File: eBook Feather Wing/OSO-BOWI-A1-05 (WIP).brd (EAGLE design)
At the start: 77.5 x 112.3 mm, 100 parts, among them IC1 MCP23008/SO, IC2 23K256-I/SN, J1 SJ-43514-SMT, Q1 IRLML0100, SW1 SPDT_SWITCH

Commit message: rename alt buttons DNP
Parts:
- renumbered BTN_NEXT_ALT to DNP_NEXT_ALT, BTN_PREV_ALT to DNP_PREV_ALT
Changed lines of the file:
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@@
 <attribute name="VALUE" x="32.9565" y="78.232" size="0.508" layer="28" font="vector" ratio="18" rot="MR270" align="center"/>
 </element>
-<element name="BTN_PREV_ALT" library="My Stuff" package="TL3330AF130QG" value="SPST_TACTILE_SWITCHRA" x="2.6416" y="91.44" smashed="yes" rot="MR90">
+<element name="DNP_PREV_ALT" library="My Stuff" package="TL3330AF130QG" value="SPST_TACTILE_SWITCHRA" x="2.6416" y="91.44" smashed="yes" rot="MR90">
 <attribute name="NAME" x="1.6256" y="95.25" size="0.508" layer="52" font="vector" ratio="18" rot="MR90" align="center"/>
 </element>
@@
 <attribute name="VALUE" x="48.768" y="64.008" size="0.4064" layer="28" ratio="10" rot="MR0"/>
 </element>
-<element name="BTN_NEXT_ALT" library="My Stuff" package="TL3330AF130QG" value="SPST_TACTILE_SWITCHRA" x="74.3204" y="90.8558" smashed="yes" rot="MR270">
+<element name="DNP_NEXT_ALT" library="My Stuff" package="TL3330AF130QG" value="SPST_TACTILE_SWITCHRA" x="74.3204" y="90.8558" smashed="yes" rot="MR270">
 <attribute name="NAME" x="75.5904" y="87.0458" size="0.508" layer="52" font="vector" ratio="18" rot="MR270" align="center"/>
 </element>
@@
 <contactref element="JP1" pad="2"/>
 <via x="45.72" y="43.18" extent="1-16" drill="0.254"/>
-<contactref element="BTN_PREV_ALT" pad="P$2"/>
-<contactref element="BTN_NEXT_ALT" pad="P$2"/>
+<contactref element="DNP_PREV_ALT" pad="P$2"/>
+<contactref element="DNP_NEXT_ALT" pad="P$2"/>
 <via x="4.572" y="18.2372" extent="1-16" drill="0.254"/>
 <via x="18.542" y="11.43" extent="1-16" drill="0.254"/>
@@
 <signal name="BTN_NEXT">
 <contactref element="IC1" pad="16"/>
-<contactref element="BTN_NEXT_ALT" pad="P$1"/>
+<contactref element="DNP_NEXT_ALT" pad="P$1"/>
 <wire x1="74.0918" y1="25.5778" x2="72.6812" y2="25.5778" width="0.1524" layer="16"/>
 <wire x1="72.6812" y1="25.5778" x2="72.672" y2="25.587" width="0.1524" layer="16"/>
@@
 </signal>
 <signal name="BTN_PREV">
-<contactref element="BTN_PREV_ALT" pad="P$1"/>
+<contactref element="DNP_PREV_ALT" pad="P$1"/>
 <contactref element="IC1" pad="15"/>
 <wire x1="2.2956" y1="93.34" x2="2.2956" y2="91.3226" width="0.1524" layer="16"/>

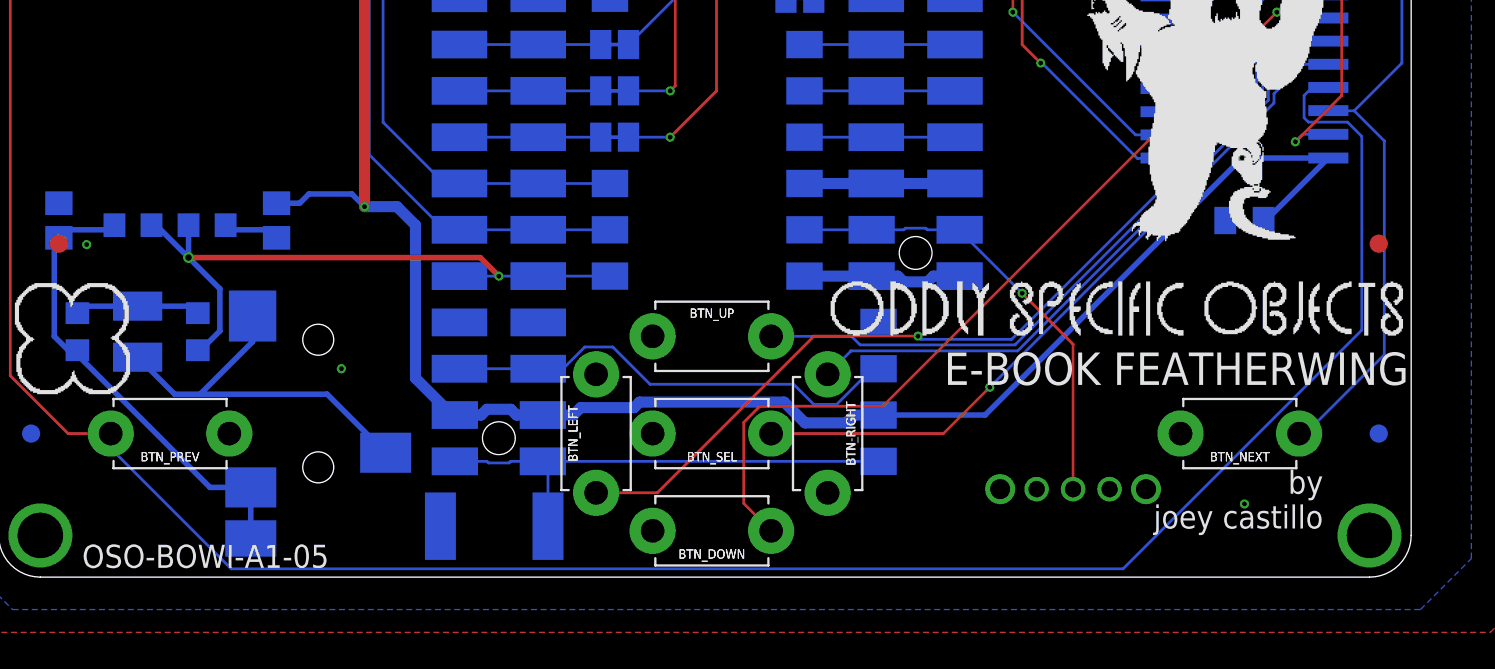
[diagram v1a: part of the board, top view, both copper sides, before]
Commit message: wing: minor silkscreen and routing tweaks
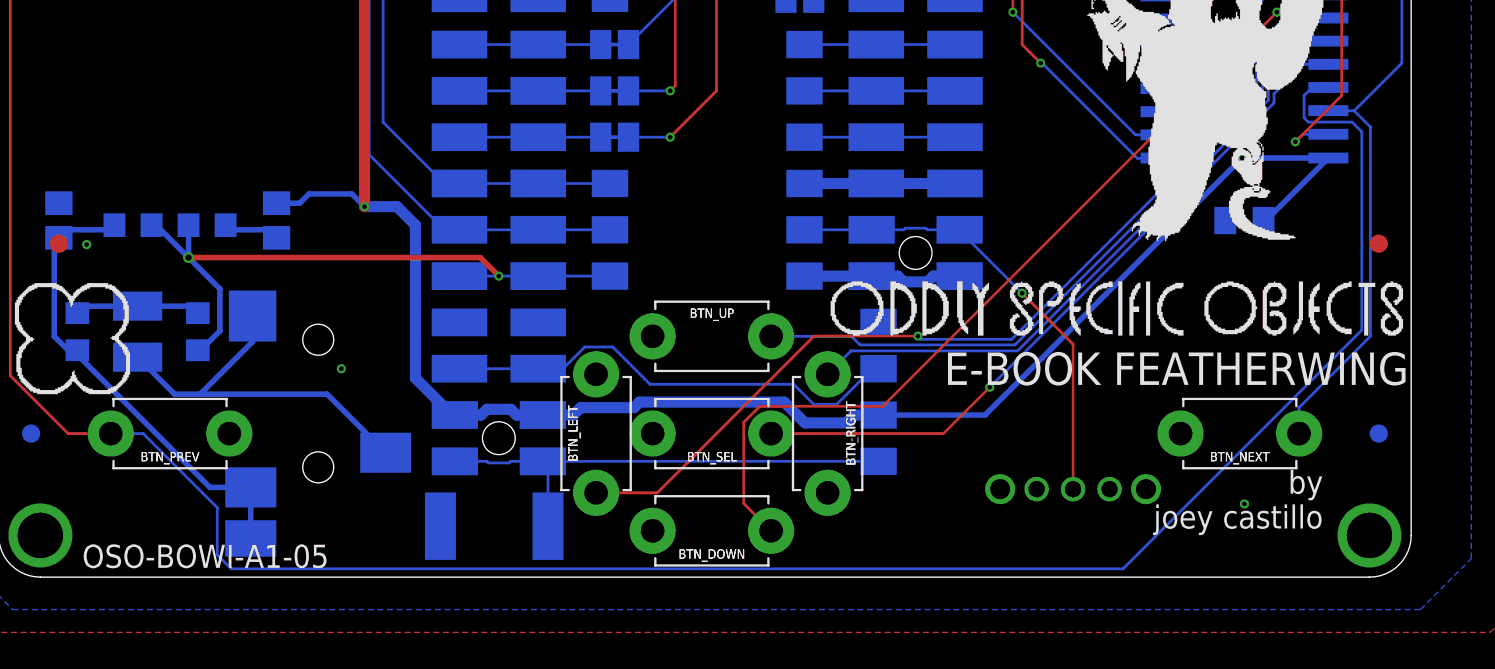
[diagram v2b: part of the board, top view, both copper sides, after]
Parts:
- renumbered FCS to BCS
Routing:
- net BTN_PREV: track 184.4 -> 185.6 mm
- net BTN_NEXT: track 89.6 -> 88.8 mm
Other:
- board text added: "BABEL FLASH CHIP"
- board text added: "If you're using a non-Express board that lacks onboard Flash, an optional GD25Q16CTIGR Flash chip can hold the entire GNU Unifont in its 2MB of memory. It uses the SPI interface, but you'll need to wire the BCS pad to a spare GPIO. If you skip this chip, omit filtering capacitor C5."
- board text removed: "2MB FLASH CHIP"
- board text removed: "If you're using a non-Express board that lacks onboard Flash, an optional GD25Q16CTIGR Flash chip can hold the entire GNU Unifont in its 2MB of memory. It uses the SPI interface, but you'll need to wire the FCS pad to a spare GPIO. If you skip this chip, omit filtering capacitor C5."
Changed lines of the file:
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@@
 <wire x1="46.736" y1="53.086" x2="46.736" y2="67.056" width="0.1524" layer="22" style="shortdash"/>
 <wire x1="46.736" y1="67.056" x2="22.606" y2="67.056" width="0.1524" layer="22" style="shortdash"/>
-<text x="76.454" y="66.294" size="1.27" layer="22" font="vector" ratio="18" rot="MR0" align="top-left">2MB FLASH CHIP</text>
+<text x="76.454" y="66.294" size="1.27" layer="22" font="vector" ratio="18" rot="MR0" align="top-left">BABEL FLASH CHIP</text>
 <text x="76.454" y="64.262" size="0.8128" layer="22" font="vector" rot="MR0" align="top-left">If you're using a non-Express
 board that lacks onboard Flash,
@@
 Unifont in its 2MB of memory. It
 uses the SPI interface, but
-you'll need to wire the FCS
+you'll need to wire the BCS
 pad to a spare GPIO. If you
 skip this chip, omit filtering capacitor C5.</text>
@@
 </element>
 <element name="SW1" library="My Stuff" package="A10767" value="SPDT_SWITCH" x="58.674" y="4.826" smashed="yes" rot="MR0">
-<attribute name="NAME" x="58.674" y="7.747" size="0.8128" layer="52" font="vector" ratio="18" rot="MR0" align="center"/>
+<attribute name="NAME" x="58.674" y="6.223" size="0.8128" layer="52" font="vector" ratio="18" rot="MR0" align="center"/>
 </element>
 <element name="U$48" library="My Stuff" package="OSO_ONELINE_125MIL" value="OSO_TEXTOSO_TEXT_ONELINE_125MIL" x="45.339" y="14.732" smashed="yes"/>
 <element name="U$44" library="My Stuff" package="OSO_GRAPHIC" value="OSO_GRAPHIC" x="3.81" y="13.081" smashed="yes"/>
 <element name="U$45" library="My Stuff" package="OSO_BEAR_750MIL" value="OSO_BEAR" x="66.1162" y="27.305" smashed="yes"/>
-<element name="FCS" library="E-Book Wing Rev C (WIP)" package="SOLDERJUMPER_OPEN" value="SOLDERJUMPER_OPEN" x="33.274" y="44.45" smashed="yes" rot="MR180">
+<element name="BCS" library="E-Book Wing Rev C (WIP)" package="SOLDERJUMPER_OPEN" value="SOLDERJUMPER_OPEN" x="33.274" y="44.45" smashed="yes" rot="MR180">
 <attribute name="NAME" x="35.56" y="44.45" size="0.508" layer="26" font="vector" ratio="18" rot="MR90" align="center"/>
 <attribute name="VALUE" x="31.75" y="46.101" size="0.4064" layer="28" ratio="10" rot="MR180"/>
@@
 <wire x1="27.740175" y1="44.5372" x2="27.827375" y2="44.45" width="0.1524" layer="16"/>
 <wire x1="27.827375" y1="44.45" x2="29.591" y2="44.45" width="0.1524" layer="16"/>
-<contactref element="FCS" pad="1"/>
+<contactref element="BCS" pad="1"/>
 <wire x1="32.512" y1="44.45" x2="29.591" y2="44.45" width="0.1524" layer="16"/>
 </signal>
@@
 <wire x1="53.34" y1="54.61" x2="52.705" y2="55.245" width="0.1524" layer="16"/>
 <wire x1="52.705" y1="55.245" x2="52.705" y2="56.074" width="0.1524" layer="16"/>
-<contactref element="FCS" pad="2"/>
+<contactref element="BCS" pad="2"/>
 <wire x1="34.036" y1="44.45" x2="33.69475" y2="44.79125" width="0.1524" layer="16"/>
 </signal>
@@
 <wire x1="76.708" y1="82.042" x2="76.708" y2="28.194" width="0.1524" layer="16"/>
 <wire x1="76.708" y1="28.194" x2="74.0918" y2="25.5778" width="0.1524" layer="16"/>
-<wire x1="75.7428" y1="23.9268" x2="75.7428" y2="12.1988" width="0.1524" layer="16"/>
-<wire x1="75.7428" y1="23.9268" x2="74.0918" y2="25.5778" width="0.1524" layer="16"/>
+<wire x1="74.9808" y1="24.6888" x2="74.9808" y2="13.2148" width="0.1524" layer="16"/>
+<wire x1="74.9808" y1="24.6888" x2="74.0918" y2="25.5778" width="0.1524" layer="16"/>
 <wire x1="74.6664" y1="88.9558" x2="72.898" y2="87.1874" width="0.1524" layer="16"/>
 <wire x1="72.898" y1="87.1874" x2="72.898" y2="84.328" width="0.1524" layer="16"/>
@@
 <wire x1="73.914" y1="83.312" x2="75.438" y2="83.312" width="0.1524" layer="16"/>
 <contactref element="BTN_NEXT" pad="P$1"/>
-<wire x1="75.7428" y1="12.1988" x2="71.418" y2="7.874" width="0.1524" layer="16"/>
-<wire x1="71.418" y1="7.874" x2="71.068" y2="7.874" width="0.1524" layer="16"/>
+<wire x1="71.068" y1="7.874" x2="71.068" y2="9.302" width="0.1524" layer="16"/>
+<wire x1="74.9808" y1="13.2148" x2="71.068" y2="9.302" width="0.1524" layer="16"/>
 </signal>
 <signal name="BTN_PREV">
@@
 <wire x1="0.381" y1="89.408" x2="0.381" y2="11.049" width="0.1524" layer="1"/>
 <wire x1="3.556" y1="7.874" x2="0.381" y2="11.049" width="0.1524" layer="1"/>
-<wire x1="12.4968" y1="0.4572" x2="5.894" y2="7.06" width="0.1524" layer="16"/>
+<wire x1="12.4968" y1="0.4572" x2="11.736" y2="1.218" width="0.1524" layer="16"/>
 <wire x1="12.4968" y1="0.4572" x2="61.4172" y2="0.4572" width="0.1524" layer="16"/>
 <wire x1="71.5789125" y1="24.9568" x2="71.3434" y2="25.1923125" width="0.1524" layer="16"/>
 <wire x1="71.3434" y1="26.416" x2="71.3434" y2="25.1923125" width="0.1524" layer="16"/>
-<wire x1="74.5086" y1="24.1736875" x2="73.7254875" y2="24.9568" width="0.1524" layer="16"/>
-<wire x1="73.7254875" y1="24.9568" x2="71.5789125" y2="24.9568" width="0.1524" layer="16"/>
-<wire x1="74.5086" y1="13.5486" x2="74.5086" y2="24.1736875" width="0.1524" layer="16"/>
+<wire x1="74.5086" y1="24.4276875" x2="73.9794875" y2="24.9568" width="0.1524" layer="16"/>
+<wire x1="73.9794875" y1="24.9568" x2="71.5789125" y2="24.9568" width="0.1524" layer="16"/>
+<wire x1="74.5086" y1="13.5486" x2="74.5086" y2="24.4276875" width="0.1524" layer="16"/>
 <wire x1="61.4172" y1="0.4572" x2="74.5086" y2="13.5486" width="0.1524" layer="16"/>
 <wire x1="72.672" y1="26.857" x2="71.7844" y2="26.857" width="0.1524" layer="16"/>
 <wire x1="71.7844" y1="26.857" x2="71.3434" y2="26.416" width="0.1524" layer="16"/>
 <contactref element="BTN_PREV" pad="P$1"/>
-<wire x1="5.894" y1="7.874" x2="5.894" y2="7.06" width="0.1524" layer="16"/>
+<wire x1="5.894" y1="7.874" x2="7.672" y2="7.874" width="0.1524" layer="16"/>
+<wire x1="11.736" y1="3.81" x2="7.672" y2="7.874" width="0.1524" layer="16"/>
+<wire x1="11.736" y1="3.81" x2="11.736" y2="1.218" width="0.1524" layer="16"/>
 <wire x1="5.894" y1="7.874" x2="3.556" y2="7.874" width="0.1524" layer="1"/>
 </signal>

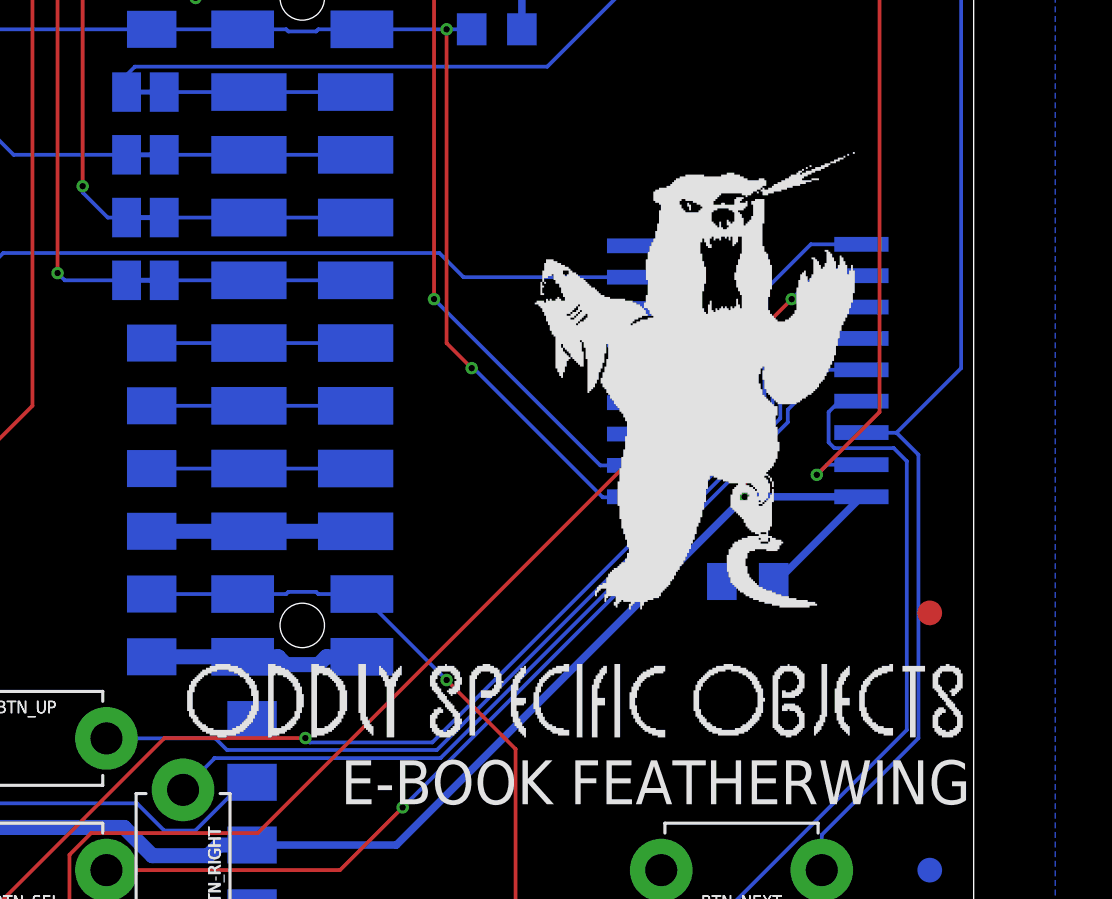
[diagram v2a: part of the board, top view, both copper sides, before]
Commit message: wing: update to higher res OSO artwork
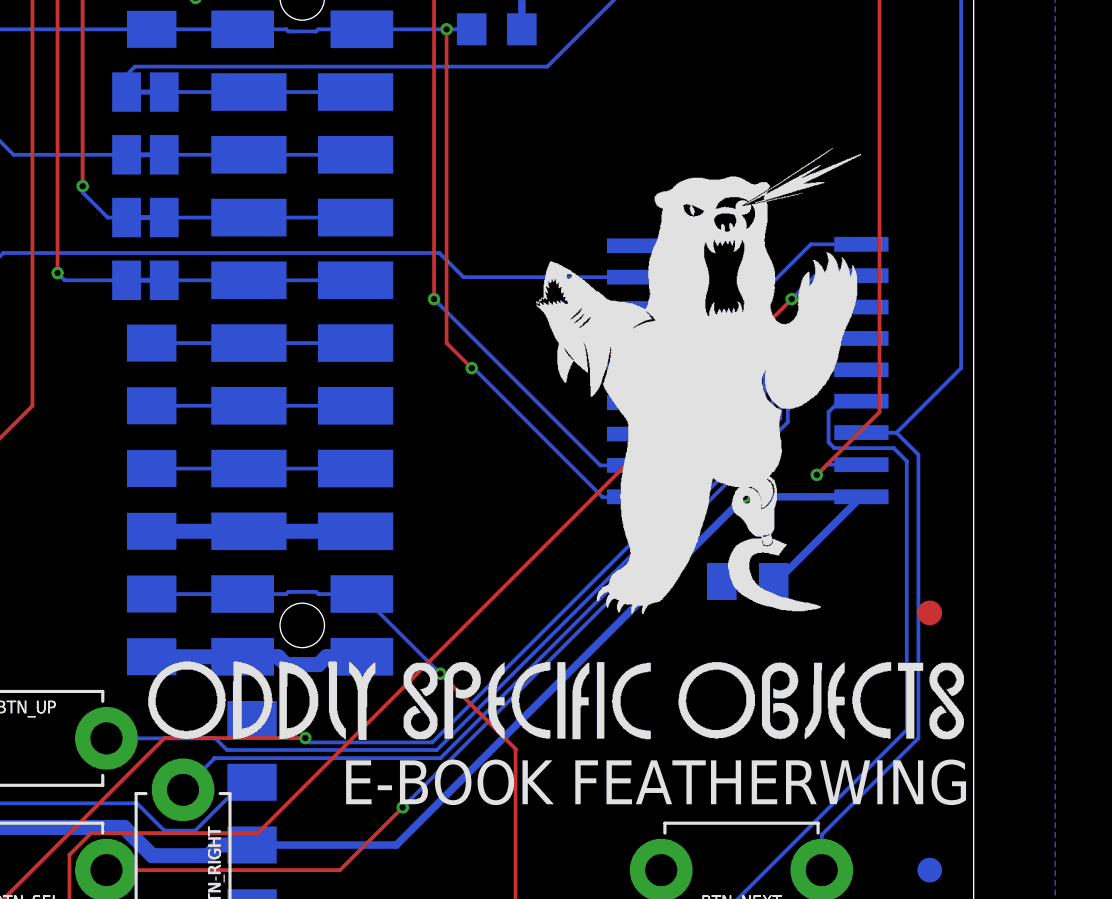
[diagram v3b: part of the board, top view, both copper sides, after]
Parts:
- removed U$45: OSO_BEAR, My Stuff:OSO_BEAR_750MIL
- removed U$48: OSO_TEXTOSO_TEXT_ONELINE_125MIL, My Stuff:OSO_ONELINE_125MIL
- added U$11: (no value), My Stuff:OSO_WORDMARK_125X1300MIL_1000DPI
- added U$8: (no value), My Stuff:OSO_BEAR_525X750MIL_1000DPI
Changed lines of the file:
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@@
 <attribute name="NAME" x="58.674" y="6.223" size="0.8128" layer="52" font="vector" ratio="18" rot="MR0" align="center"/>
 </element>
-<element name="U$48" library="My Stuff" package="OSO_ONELINE_125MIL" value="OSO_TEXTOSO_TEXT_ONELINE_125MIL" x="45.339" y="14.732" smashed="yes"/>
 <element name="U$44" library="My Stuff" package="OSO_GRAPHIC" value="OSO_GRAPHIC" x="3.81" y="13.081" smashed="yes"/>
-<element name="U$45" library="My Stuff" package="OSO_BEAR_750MIL" value="OSO_BEAR" x="66.1162" y="27.305" smashed="yes"/>
 <element name="BCS" library="E-Book Wing Rev C (WIP)" package="SOLDERJUMPER_OPEN" value="SOLDERJUMPER_OPEN" x="33.274" y="44.45" smashed="yes" rot="MR180">
 <attribute name="NAME" x="35.56" y="44.45" size="0.508" layer="26" font="vector" ratio="18" rot="MR90" align="center"/>
@@
 <attribute name="VALUE" x="34.9" y="79.216" size="0.8128" layer="28" ratio="12" rot="MR270"/>
 </element>
+<element name="U$8" library="My Stuff" package="OSO_BEAR_525X750MIL_1000DPI" value="" x="66.04" y="27.686" smashed="yes"/>
+<element name="U$11" library="My Stuff" package="OSO_WORDMARK_125X1300MIL_1000DPI" value="" x="43.815" y="14.732" smashed="yes"/>
 </elements>
 <signals>
@@
 <wire x1="49.388625" y1="19.05" x2="47.625" y2="19.05" width="0.1524" layer="16"/>
 <wire x1="47.625" y1="19.05" x2="43.942" y2="19.05" width="0.1524" layer="16"/>
-<via x="55.88" y="15.5702" extent="1-16" drill="0.254"/>
+<via x="55.626" y="15.8242" extent="1-16" drill="0.254"/>
 <wire x1="52.451" y1="19.05" x2="52.451" y2="18.9992" width="0.1524" layer="16"/>
-<wire x1="55.88" y1="15.5702" x2="52.451" y2="18.9992" width="0.1524" layer="16"/>
-<wire x1="55.88" y1="15.5702" x2="58.674" y2="12.7762" width="0.1524" layer="1"/>
+<wire x1="55.626" y1="15.8242" x2="52.451" y2="18.9992" width="0.1524" layer="16"/>
+<wire x1="55.626" y1="15.8242" x2="58.674" y2="12.7762" width="0.1524" layer="1"/>
 <contactref element="SW1" pad="P$2"/>
 <wire x1="58.674" y1="12.7762" x2="58.674" y2="4.826" width="0.1524" layer="1"/>
